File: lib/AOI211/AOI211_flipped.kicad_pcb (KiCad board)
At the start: 2 copper layers, 8 parts

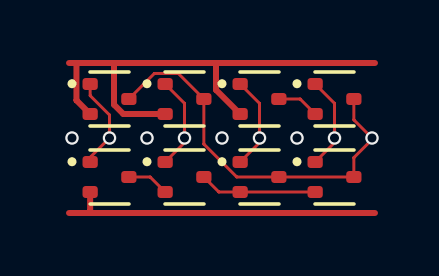
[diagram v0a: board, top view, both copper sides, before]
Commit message: High-density layout with pitch of 1.1mm, which gains 23% !!
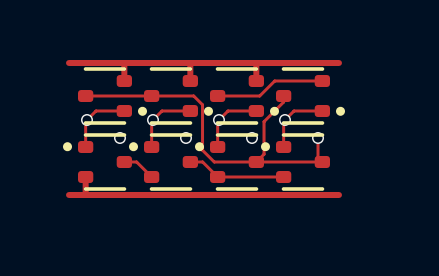
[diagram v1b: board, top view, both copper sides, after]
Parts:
- moved P4 1.16 mm to (7.70, 3.30)
- moved N4 1.05 mm to (7.70, 1.10), turned to 180 degrees
- moved P3 0.90 mm to (5.50, 3.30)
- moved N3 0.76 mm to (5.50, 1.10), turned to 180 degrees
- moved P2 0.67 mm to (3.30, 3.30)
- moved P1 0.52 mm to (1.10, 3.30)
- moved N2 0.46 mm to (3.30, 1.10), turned to 180 degrees
- moved N1 0.18 mm to (1.10, 1.10), turned to 180 degrees
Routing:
- net GND: track 17.4 -> 10.8 mm
- net intC: track 1.42 -> 3.70 mm
- net VDD: track 10.9 -> 9.61 mm
- net C1: track 3.13 -> 2.29 mm
- net B: track 3.13 -> 2.29 mm
- net A: track 3.13 -> 2.29 mm
- net C2: track 3.13 -> 2.29 mm
- net intPB: track 3.92 -> 3.32 mm
- net (no net): vias 4 -> 3

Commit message: All cells now use 1mm*4mm grid rather than 1.1mm*4.4mm
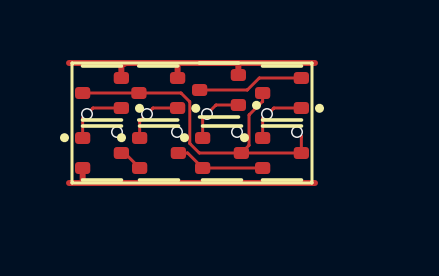
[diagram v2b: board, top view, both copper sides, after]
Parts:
- moved P4 0.76 mm to (7.00, 3.00)
- moved N4 0.71 mm to (7.00, 1.00)
- moved N3 0.63 mm to (4.90, 0.90)
- moved P3 0.58 mm to (5.00, 3.00)
- moved P2 0.50 mm to (2.90, 3.00)
- moved N2 0.44 mm to (2.88, 1.00)
- moved P1 0.32 mm to (1.00, 3.00)
- moved N1 0.14 mm to (1.00, 1.00)
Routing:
- net GND: track 10.8 -> 9.69 mm
- net Y: track 13.1 -> 12.0 mm
- net VDD: track 9.61 -> 8.72 mm

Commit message: Make the pads of my SOT523 footprint very slightly smaller, which is enough to route all the cells and leave the mosfets exactly on the grid
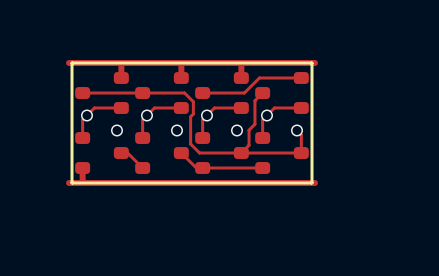
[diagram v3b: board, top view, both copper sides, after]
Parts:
- N1, N2, N3, N4, P1, P2, P3, P4: footprint Package_TO_SOT_SMD:SOT-523 -> RV523:SOT523
- moved N3 0.14 mm to (5.00, 1.00)
- moved N2 0.12 mm to (3.00, 1.00)
- moved P2 0.10 mm to (3.00, 3.00)

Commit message: Propagate MOSFET values to the cells' PCBs
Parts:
- N1, N2, N3, N4: value (none) -> NMOS
- P1, P2, P3, P4: value (none) -> PMOS
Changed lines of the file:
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@@
 			)
 		)
-		(property "Value" ""
+		(property "Value" "PMOS"
 			(at 0 0 0)
 			(layer "F.Fab")
@@
 			)
 		)
-		(property "Value" ""
+		(property "Value" "NMOS"
 			(at 0 0 180)
 			(layer "F.Fab")
@@
 			)
 		)
-		(property "Value" ""
+		(property "Value" "PMOS"
 			(at 0 0 0)
 			(layer "F.Fab")
@@
 			)
 		)
-		(property "Value" ""
+		(property "Value" "PMOS"
 			(at 0 0 0)
 			(layer "F.Fab")
@@
 			)
 		)
-		(property "Value" ""
+		(property "Value" "NMOS"
 			(at 0 0 180)
 			(layer "F.Fab")
@@
 			)
 		)
-		(property "Value" ""
+		(property "Value" "NMOS"
 			(at 0 0 180)
 			(layer "F.Fab")
@@
 			)
 		)
-		(property "Value" ""
+		(property "Value" "PMOS"
 			(at 0 0 0)
 			(layer "F.Fab")
@@
 			)
 		)
-		(property "Value" ""
-			(at 0 0 180)
-			(layer "F.Fab")
+		(property "Value" "NMOS"
+			(at 0 0 180)
+			(layer "F.Fab")
